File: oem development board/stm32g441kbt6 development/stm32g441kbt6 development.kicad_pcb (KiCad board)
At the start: 2 copper layers, 50 x 30.3 mm, 50 parts, among them J1 CONN_pcie_x1, J2 Programming_Pin_Header, SW1 INTERRUPT TEST SWITCH, U1 STM32G441KBT6, U2 MCP2561-E_SN, U3 AP63203WU-7, Y1 X_Crystal_16MHz_18pF

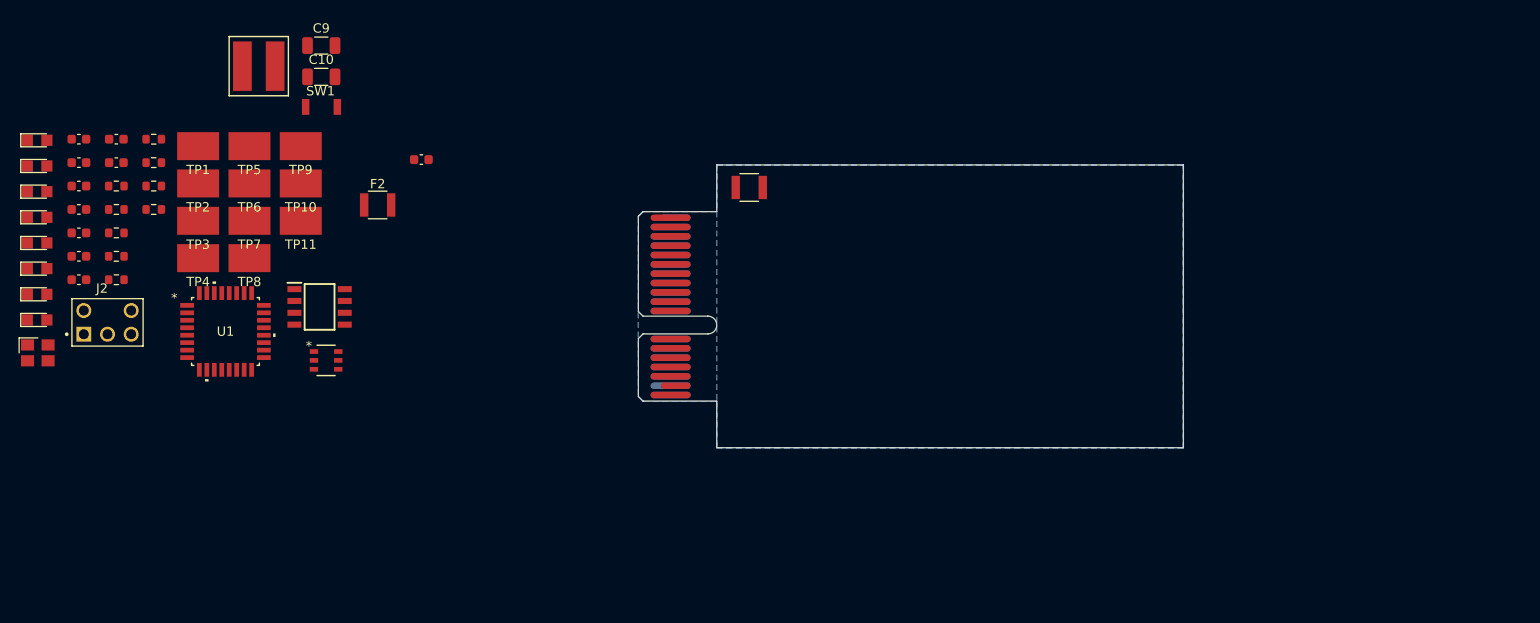
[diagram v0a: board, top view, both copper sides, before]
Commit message: Added 3D Models, Started PCB Design, Minor Fixes to Schematics
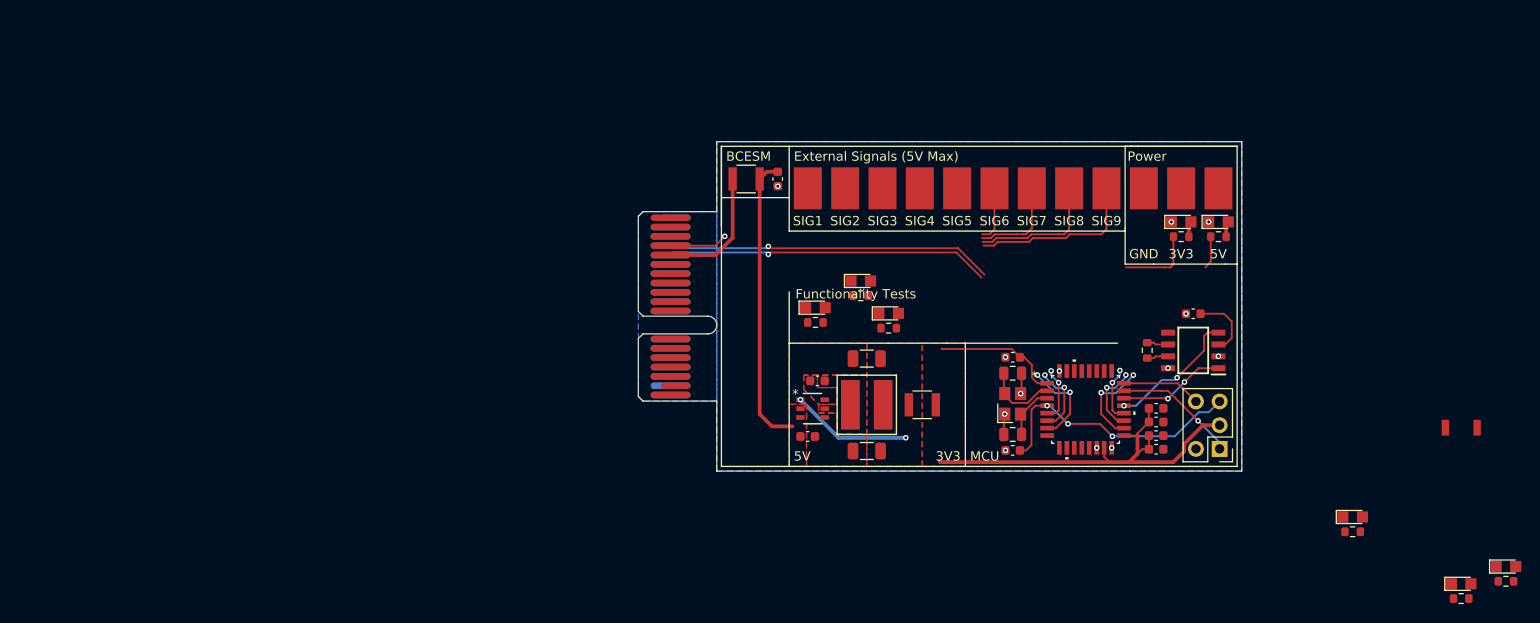
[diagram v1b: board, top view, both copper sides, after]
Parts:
- added C13: C_18pF, Capacitor_SMD:C_0805_2012Metric, F.Cu at (149.1, 87.2)
- added C14: C_18pF, Capacitor_SMD:C_0805_2012Metric, F.Cu at (149.1, 93.8)
- added TP12: GND, OEM:Test_Point_SMD, F.Cu at (163.1, 67.4)
- moved D4 161.8 mm to (201.9, 108.0)
- moved D5 156.9 mm to (197.1, 109.8)
- moved R5 152.4 mm to (201.9, 109.5)
- moved R6 148.5 mm to (197.1, 111.4)
- moved D3 145.2 mm to (185.5, 102.6)
- moved R4 135.7 mm to (185.5, 104.2)
- moved SW1 126.9 mm to (195.4, 93.1)
- moved D2 126.7 mm to (171.1, 71.0)
- moved D1 122.9 mm to (167.1, 71.0)
- moved C1 120.9 mm to (168.4, 80.9)
- moved J2 119.9 mm to (171.2, 95.3), turned to 180 degrees
- moved C3 118.5 mm to (164.4, 93.9)
- moved C4 118.3 mm to (164.4, 95.4)
- moved R3 118.1 mm to (171.1, 72.6)
- moved C5 117.2 mm to (164.4, 92.5)
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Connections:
- C10 pad 1: Net-(C10-Pad1) -> Net-(U3-FB)
- C3 pad 2: Net-(C3-Pad2) -> GND
- C4 pad 1: Net-(C3-Pad2) -> +3V3
- C5 pad 2: Net-(C5-Pad2) -> GND
- C6 pad 1: Net-(C5-Pad2) -> +3V3
- C6 pad 2: Net-(C6-Pad2) -> GND
- C7 pad 1: Net-(C6-Pad2) -> +3V3
- C9 pad 2: Net-(C10-Pad1) -> GND
- J1 pad A2: Net-(J1-5V) -> unconnected-(J1-3.3V-PadA2)
- J1 pad B5: unconnected-(J1-3.3V-PadB5) -> Net-(J1-5V)
- R7 pad 1: GND -> /INTERRUPT_TEST_HW
- SW1 pad 2: GND -> /INTERRUPT_TEST_HW
- U1 pad 5: GND -> /INTERRUPT_TEST_HW
- U1 pad 6: unconnected-(U1-(TIM15_CH1N/TIM2_CH2/GPIO_EXTI1/ADC2_IN2/ADC1_IN2)PA1*-Pad6) -> /HEARTBEAT
- Y1 pad 1: Net-(U1-PF0-OSC_IN) -> Net-(U1-PF1-OSC_OUT)
- Y1 pad 3: Net-(U1-PF1-OSC_OUT) -> Net-(U1-PF0-OSC_IN)
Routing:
- net +3V3: track 0.00 -> 66.7 mm
- net +5V: track 0.00 -> 42.2 mm
- net /CAN_+: track 0.00 -> 37.4 mm, vias 0 -> 1
- net /CAN_-: track 0.00 -> 37.0 mm, vias 0 -> 1
- net /NRST: track 0.00 -> 28.5 mm, vias 0 -> 3
- net /EXTERNAL_SIGNAL_9: track 0.00 -> 18.3 mm
- net /CAN_RX: track 0.00 -> 14.3 mm, vias 0 -> 2
- net /EXTERNAL_SIGNAL_8: track 0.00 -> 14.2 mm
- net Net-(J1-5V): track 0.00 -> 13.7 mm
- net /SWDIO: track 0.00 -> 13.3 mm, vias 0 -> 1
- net Net-(U3-FB): track 0.00 -> 13.0 mm, vias 0 -> 2
- net /CAN_TX: track 0.00 -> 11.5 mm, vias 0 -> 2
- net GND: track 0.00 -> 10.8 mm, vias 0 -> 14
- net /EXTERNAL_SIGNAL_7: track 0.00 -> 10.1 mm
- net /PWM_TEST: track 0.00 -> 9.77 mm, vias 0 -> 2
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- added copper zone on F.Cu, net +3V3
- added copper zone on F.Cu, net +5V
- added copper zone on F.Cu, net GND
- added copper zone on F.Cu, net Net-(U3-BST)
- added copper zone on F.Cu, net Net-(U3-FB)
- added copper zone on F.Cu, net Net-(U3-SW)
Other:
- board size 50 x 30.3 mm -> 56.3 x 35.3 mm
- board text added: "3V3"
- board text added: "5V"
- board text added: "BCESM"
- board text added: "External Signals (5V Max)"
- board text added: "Functionality Tests"
- board text added: "GND"
- board text added: "MCU"
- board text added: "Power"
- board text added: "SIG1"
- board text added: "SIG2"
- board text added: "SIG3"
- board text added: "SIG4"
- board text added: "SIG5"
- board text added: "SIG6"
- board text added: "SIG7"
- board text added: "SIG8"
- board text added: "SIG9"

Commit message: Finished PCB Design
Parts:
- added REF**: OEM_Logo_8mm, OEM:OEM_Logo_8mm, B.Cu at (169.1, 66.9)
- moved SW1 75.7 mm to (119.8, 93.7)
- moved D4 63.6 mm to (144.9, 79.7)
- moved R5 63.6 mm to (144.9, 81.3)
- moved D5 56.1 mm to (149.8, 79.7)
- moved R6 56.1 mm to (149.8, 81.3)
- moved D3 37.6 mm to (155.7, 79.7)
- moved R4 37.6 mm to (155.7, 81.3)
- moved R7 7.74 mm to (128.1, 81.3)
- moved D6 7.74 mm to (128.1, 79.7)
- moved D8 6.57 mm to (138.9, 79.7)
- moved R9 6.57 mm to (138.9, 81.3)
- moved R8 5.61 mm to (133.5, 81.3)
- moved D7 5.61 mm to (133.5, 79.7)
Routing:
- net /EXTERNAL_SIGNAL_1: track 7.52 -> 80.1 mm, vias 2 -> 5
- net /EXTERNAL_SIGNAL_2: track 5.97 -> 78.1 mm, vias 2 -> 6
- net /EXTERNAL_SIGNAL_4: track 0.00 -> 72.1 mm, vias 0 -> 4
- net /EXTERNAL_SIGNAL_5: track 0.00 -> 72.0 mm, vias 0 -> 3
- net /EXTERNAL_SIGNAL_3: track 0.00 -> 71.9 mm, vias 0 -> 3
- net +5V: track 42.2 -> 114.0 mm, vias 0 -> 4
- net +3V3: track 66.7 -> 137.0 mm, vias 0 -> 6
- net /EXTERNAL_SIGNAL_6: track 5.93 -> 72.2 mm, vias 0 -> 4
- net /EXTERNAL_SIGNAL_7: track 10.1 -> 72.1 mm, vias 0 -> 3
- net /EXTERNAL_SIGNAL_8: track 14.2 -> 74.2 mm, vias 0 -> 3
- net /EXTERNAL_SIGNAL_9: track 18.3 -> 77.5 mm, vias 0 -> 3
- net /INTERRUPT_TEST_HW: track 5.93 -> 51.1 mm, vias 2 -> 4
- net /INTERRUPT_TEST_SW: track 9.67 -> 37.3 mm, vias 2 -> 4
- net /CAN_-: track 37.0 -> 59.3 mm, vias 1 -> 3
- net /CAN_+: track 37.4 -> 59.2 mm, vias 1 -> 5
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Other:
- board text added: "<3"
- board text added: "EI TEST"
- board text added: "EI_HW"
- board text added: "EI_SW"
- board text added: "NRST"
- board text added: "PWM"
- board text added: "SWDIO"
- board text removed: "Functionality Tests"

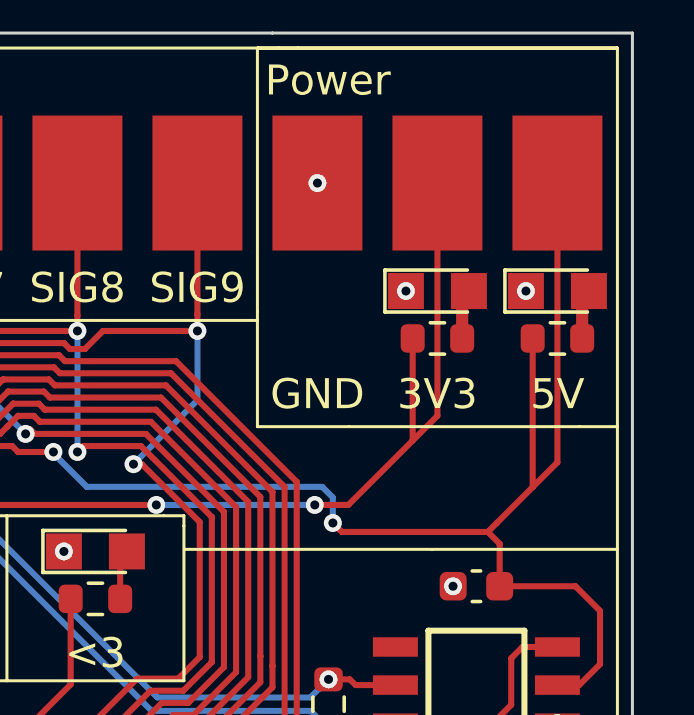
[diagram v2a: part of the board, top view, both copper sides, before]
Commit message: Added Datasheet References, Minor PCB Design Changes
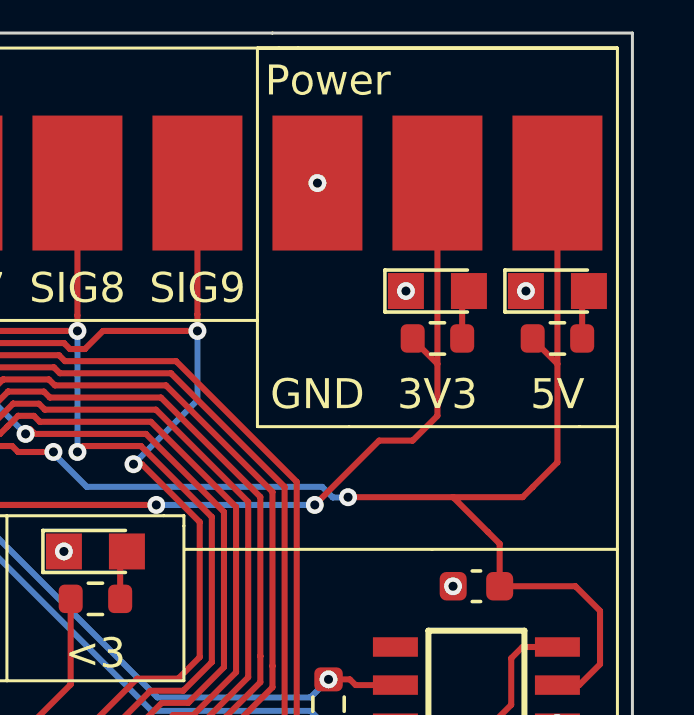
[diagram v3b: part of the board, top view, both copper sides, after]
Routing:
- net +5V: track 114.0 -> 110.4 mm
- net +3V3: track 137.0 -> 134.7 mm

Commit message: Added Minor PCB Cosmetic and Schematic Things
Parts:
- added kibuzzard-68A62DAB: G***, kibuzzard-68A62DAB, B.Cu at (154.0, 64.1)
- added kibuzzard-68A62DD1: G***, kibuzzard-68A62DD1, B.Cu at (150.8, 66.9)
- added kibuzzard-68A62E54: G***, kibuzzard-68A62E54, B.Cu at (158.7, 69.8)
